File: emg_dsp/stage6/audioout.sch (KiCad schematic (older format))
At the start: 17 parts, among them U94 MIC5365-2.5, U95 AD5663, U96 LM4808, U97 AUDIO_JACK

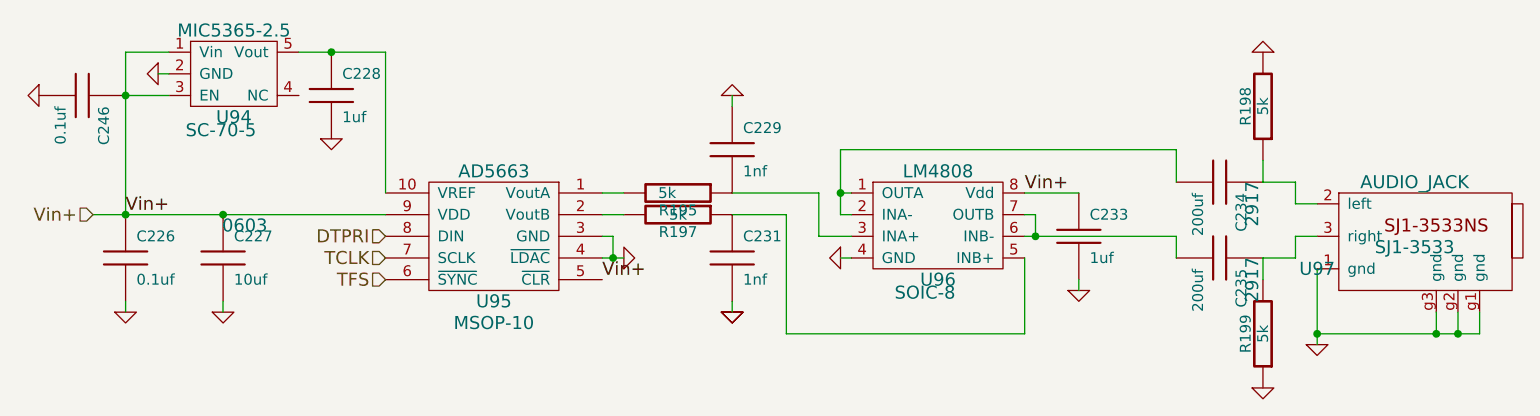
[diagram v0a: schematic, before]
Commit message: getting the last of the nets (GND, Vdd, Vcc) routed. still need to check the pinouts, etc.
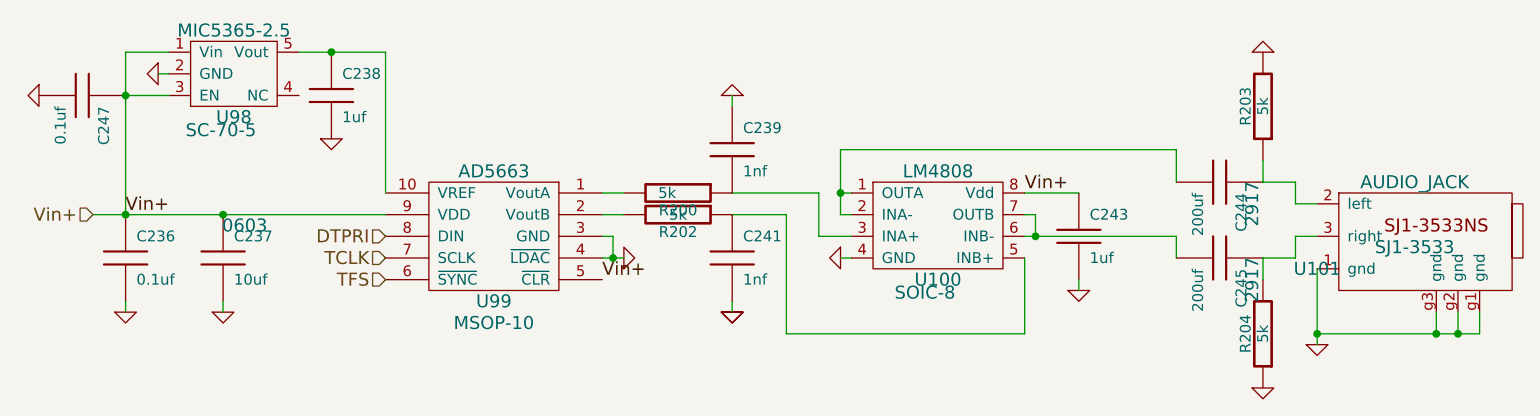
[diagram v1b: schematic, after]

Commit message: silkscreen mostly done, the board is very nearly finished!!
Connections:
- net Vin+ renamed VDD
